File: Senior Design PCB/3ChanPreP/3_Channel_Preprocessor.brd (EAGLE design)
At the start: 73.3 x 38.1 mm, 85 parts, among them U1 AD8613AUJZ-R2, U2 AD8619ARZ, U3 AD8613AUJZ-R2, U4 AD8619ARZ, U5 AD8613AUJZ-R2, U6 AD8619ARZ

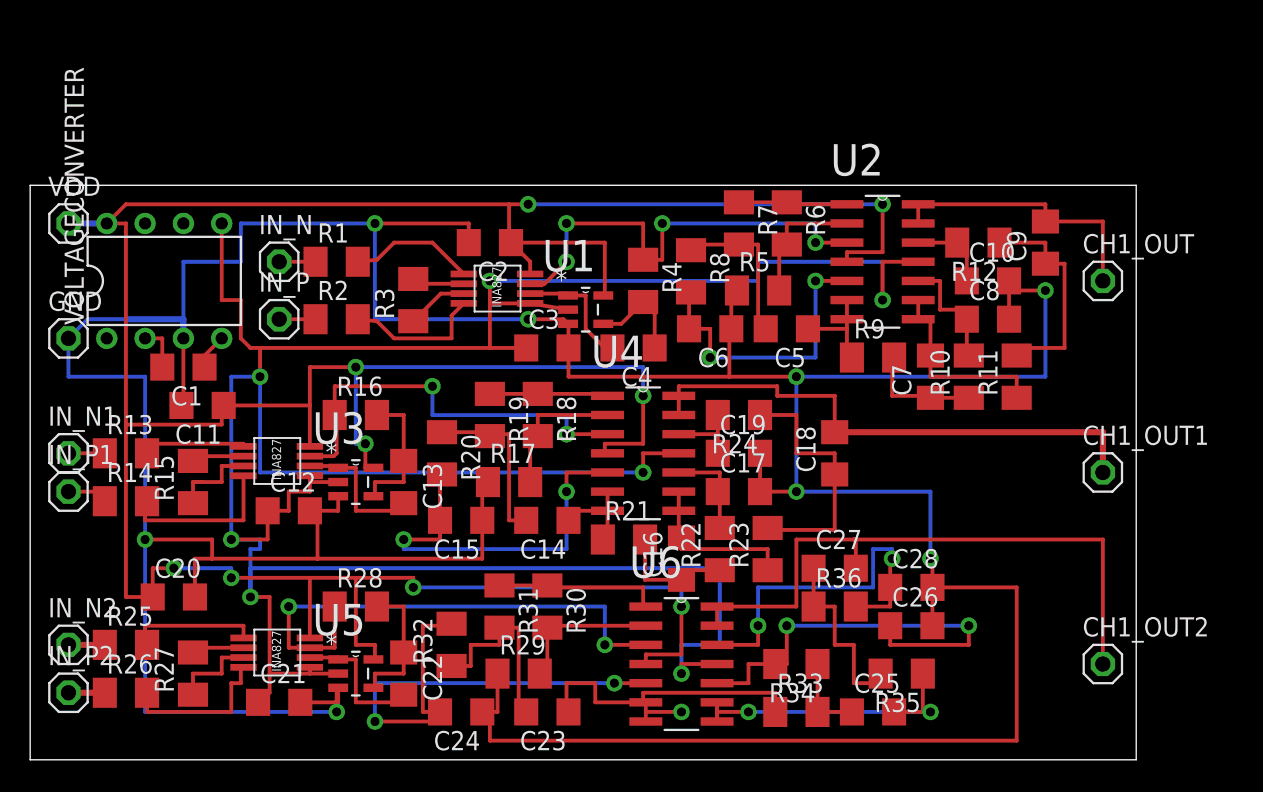
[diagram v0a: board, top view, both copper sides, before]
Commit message: Added BOMs, versions for assembly instructions
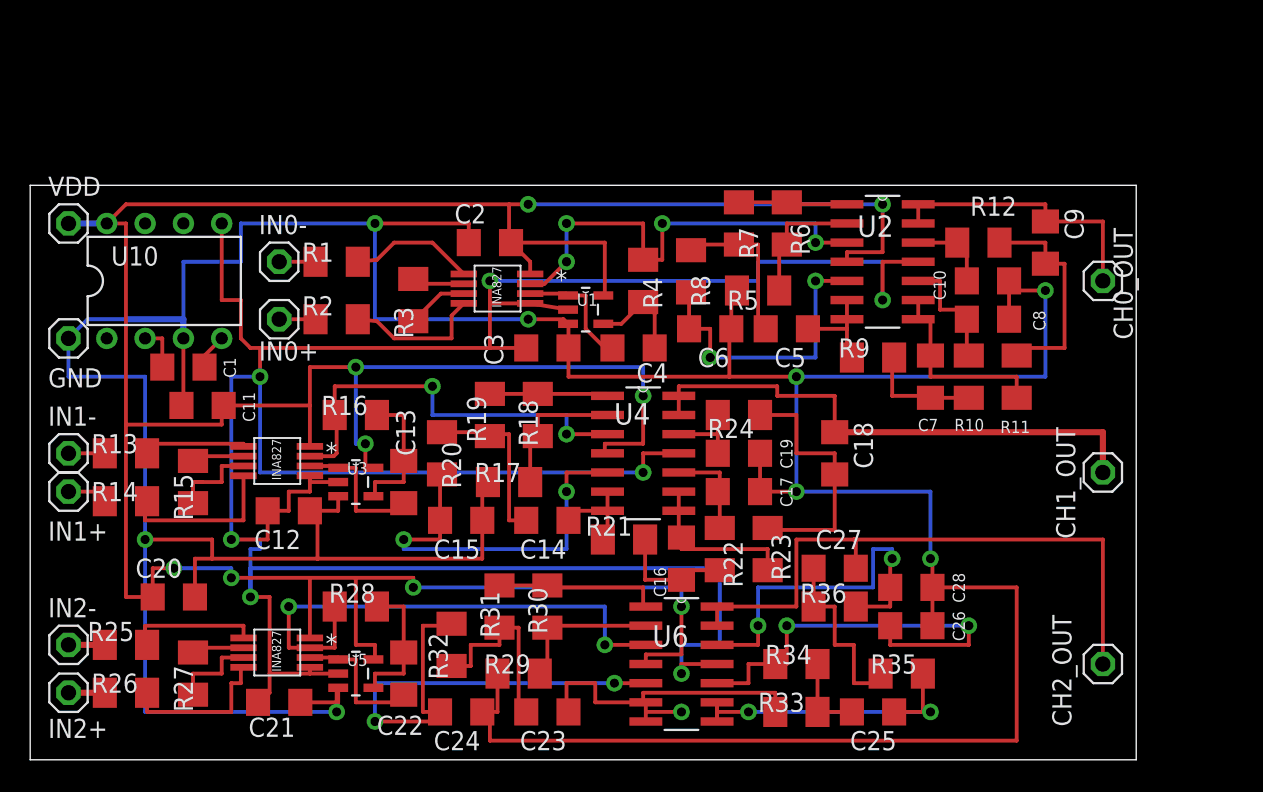
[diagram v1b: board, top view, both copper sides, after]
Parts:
- removed CH1_OUT1: (no value), pinhead:1X01
- added CH0_OUT: (no value), pinhead:1X01
- moved CH1_OUT 12.7 mm to (71.1, 61.0)
- renumbered CH1_OUT2 to CH2_OUT, INA1 to U9, IN_N to IN0-, IN_N1 to IN1-, IN_N2 to IN2-, IN_P to IN0+, IN_P1 to IN1+, IN_P2 to IN2+, VOLTAGECONVERTER to U10
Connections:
- net OUT_D: now also CH0_OUT.1; no longer CH1_OUT.1
- net OUT_D1: now also CH1_OUT.1; no longer CH1_OUT1.1
